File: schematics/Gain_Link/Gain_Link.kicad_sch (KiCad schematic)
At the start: 12 parts, among them IC1 AD8221TRMZ-EP, J1 PCIE-036-02-X-D-TH, J2 Conn_01x05_Socket

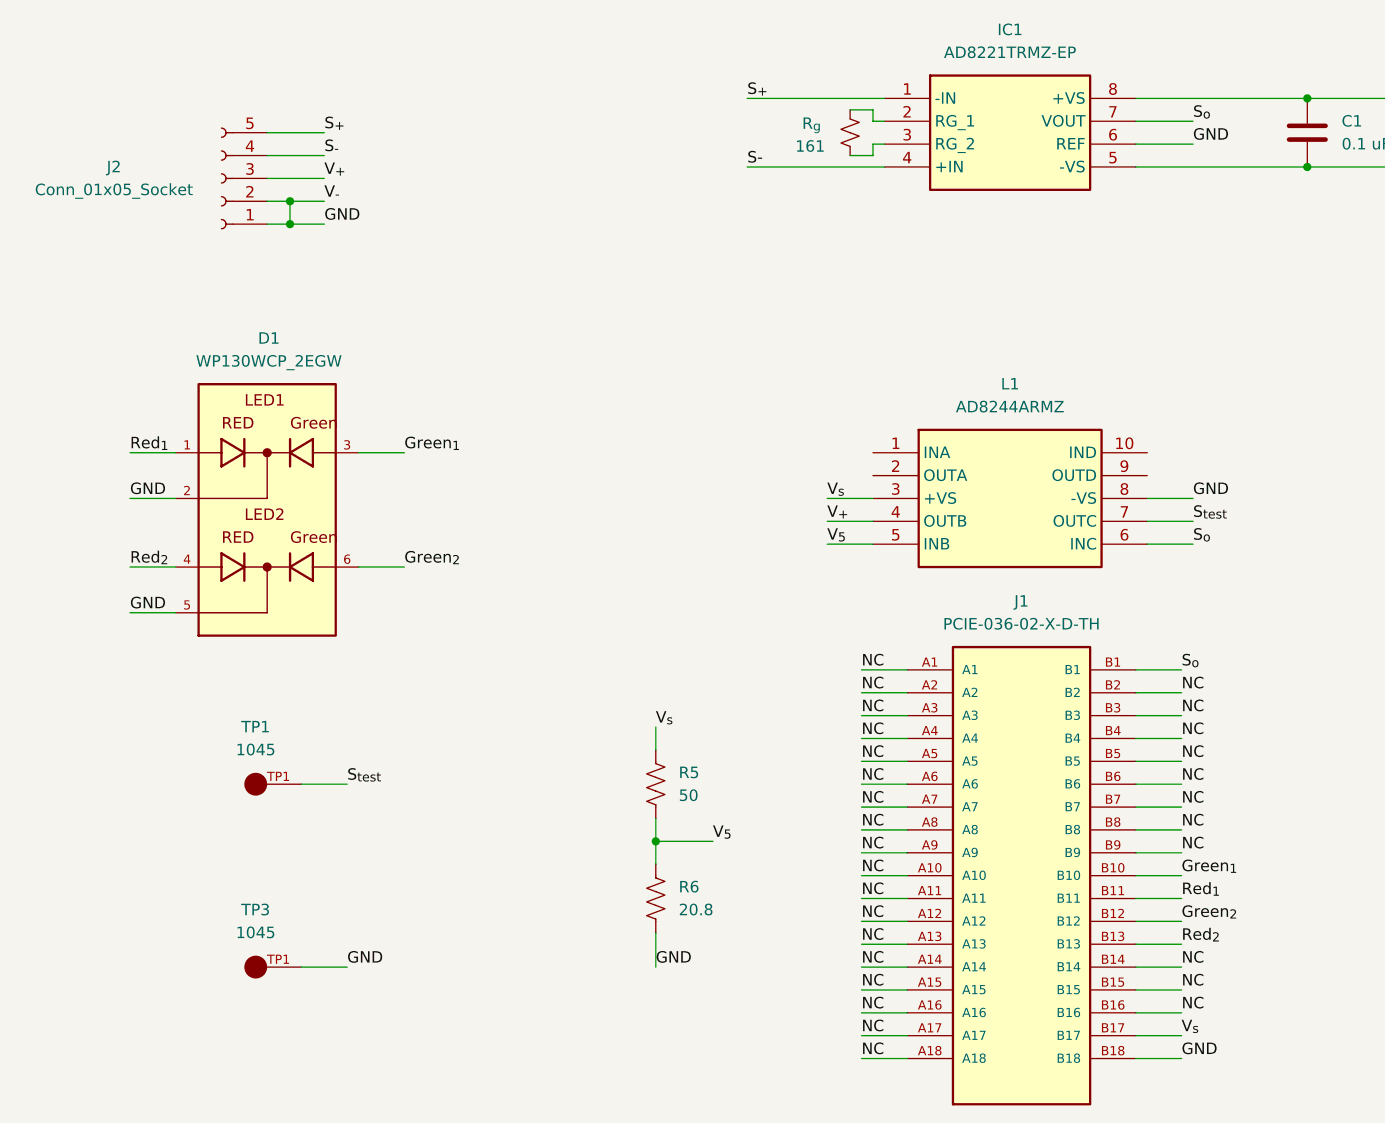
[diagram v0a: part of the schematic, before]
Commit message: Updated LP_breakout
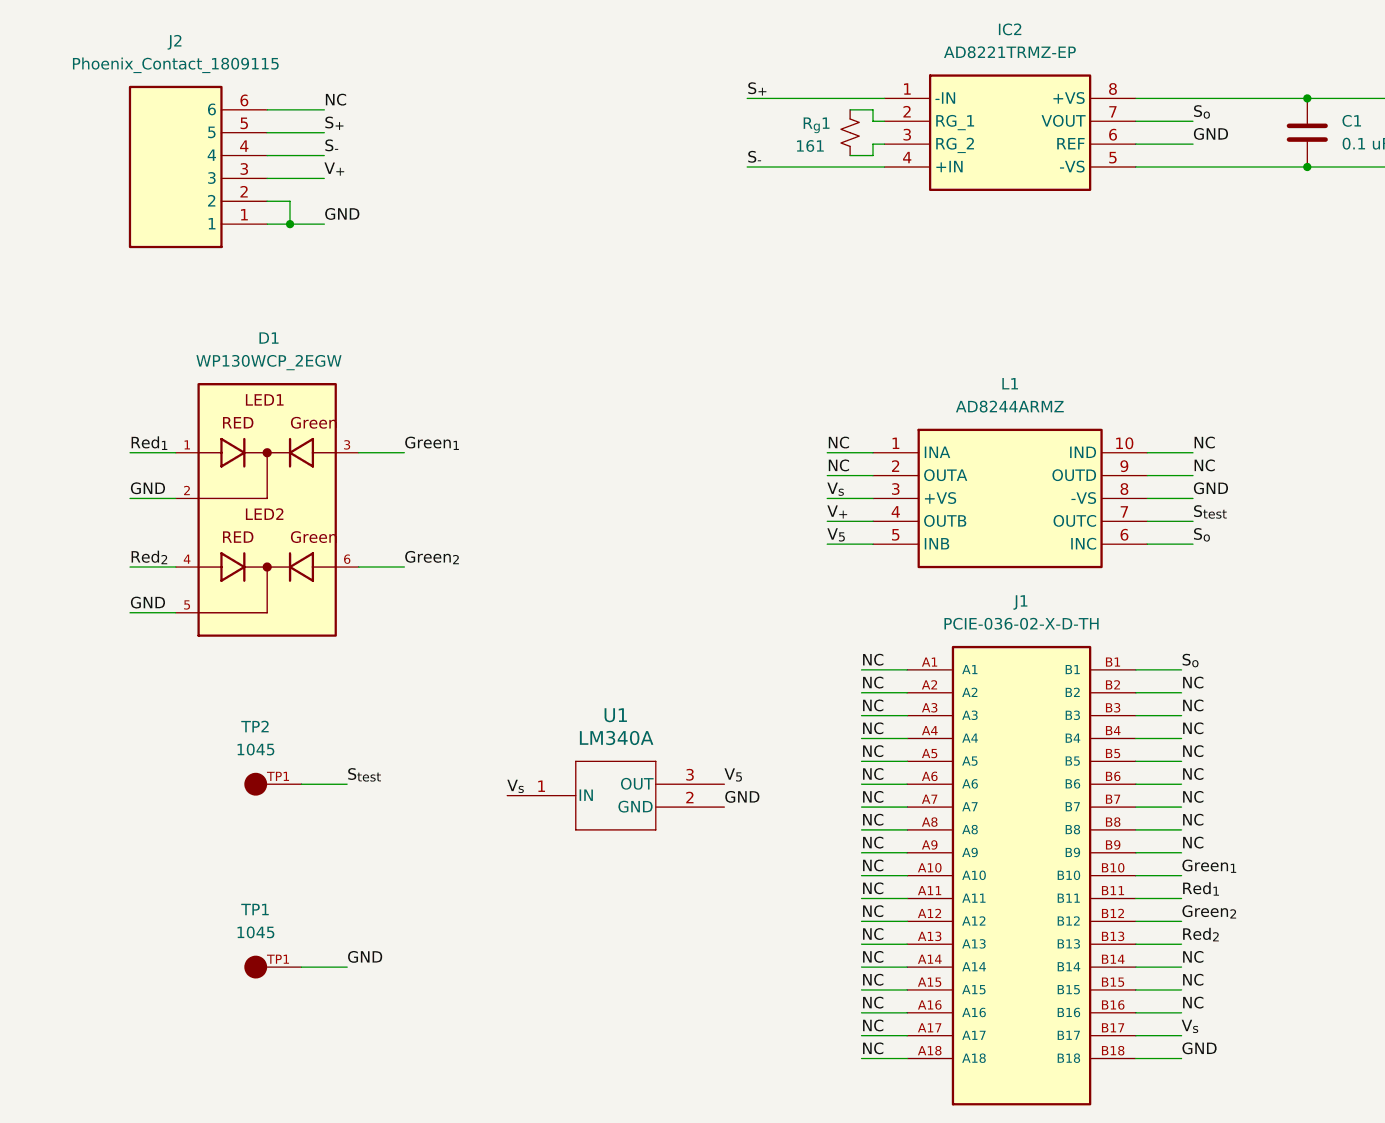
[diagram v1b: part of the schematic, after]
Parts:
- removed IC1: AD8221TRMZ-EP, Link_Footprints:AD8221TRMZ-EP, symbol Link_Components:AD8221TRMZ-EP
- removed J2: Conn_01x05_Socket, Link_Footprints:Phoenix_Contact_MSTBA,5-LR, symbol Connector:Conn_01x05_Socket
- removed R5: 50, Resistor_SMD:R_0805_2012Metric, symbol Device:R_US
- removed R6: 20.8, Resistor_SMD:R_0805_2012Metric, symbol Device:R_US
- removed TP3: 1045, Link_Footprints:Keystone_1045, symbol Link_Components:1045
- added IC2: AD8221TRMZ-EP, symbol Link_Components:AD8221TRMZ-EP
- added J2: Phoenix_Contact_1809115, symbol Link_Components:Phoenix_Contact_1809115
- added TP2: 1045, symbol Link_Components:1045
- added U1: LM340A, T03B_TEX, symbol Link_Components:LM340A
- D1: footprint Link_Footprints:LED_Lights -> (none)
- J1: footprint Link_Footprints:SAMTEC_PCIE_1x -> (none)
- L1: footprint Link_Footprints:AD8244ARMZ -> (none)
- TP1: footprint Link_Footprints:Keystone_1045 -> (none)
- renumbered R_{g} to R_{g}1
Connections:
- net GND: now also TP1.TP1, IC2.5 (-VS), IC2.6 (REF), J2.1, J2.2, U1.2 (GND)
- net NC: now also L1.1 (INA), L1.10 (IND), L1.2 (OUTA), L1.9 (OUTD), J2.6
- net S_{+}: now also IC2.1 (-IN), J2.5
- net S_{-}: now also IC2.4 (+IN), J2.4
- net S_{o}: now also IC2.7 (VOUT)
- net S_{test}: now also TP2.TP1; no longer TP1.TP1
- net V_{+}: now also J2.3
- net V_{5}: now also U1.3 (OUT)
- net V_{s}: now also IC2.8 (+VS), U1.1 (IN)
- net at R_{g}1.1: now also IC2.2 (RG_1)
- net at R_{g}1.2: now also IC2.3 (RG_2)

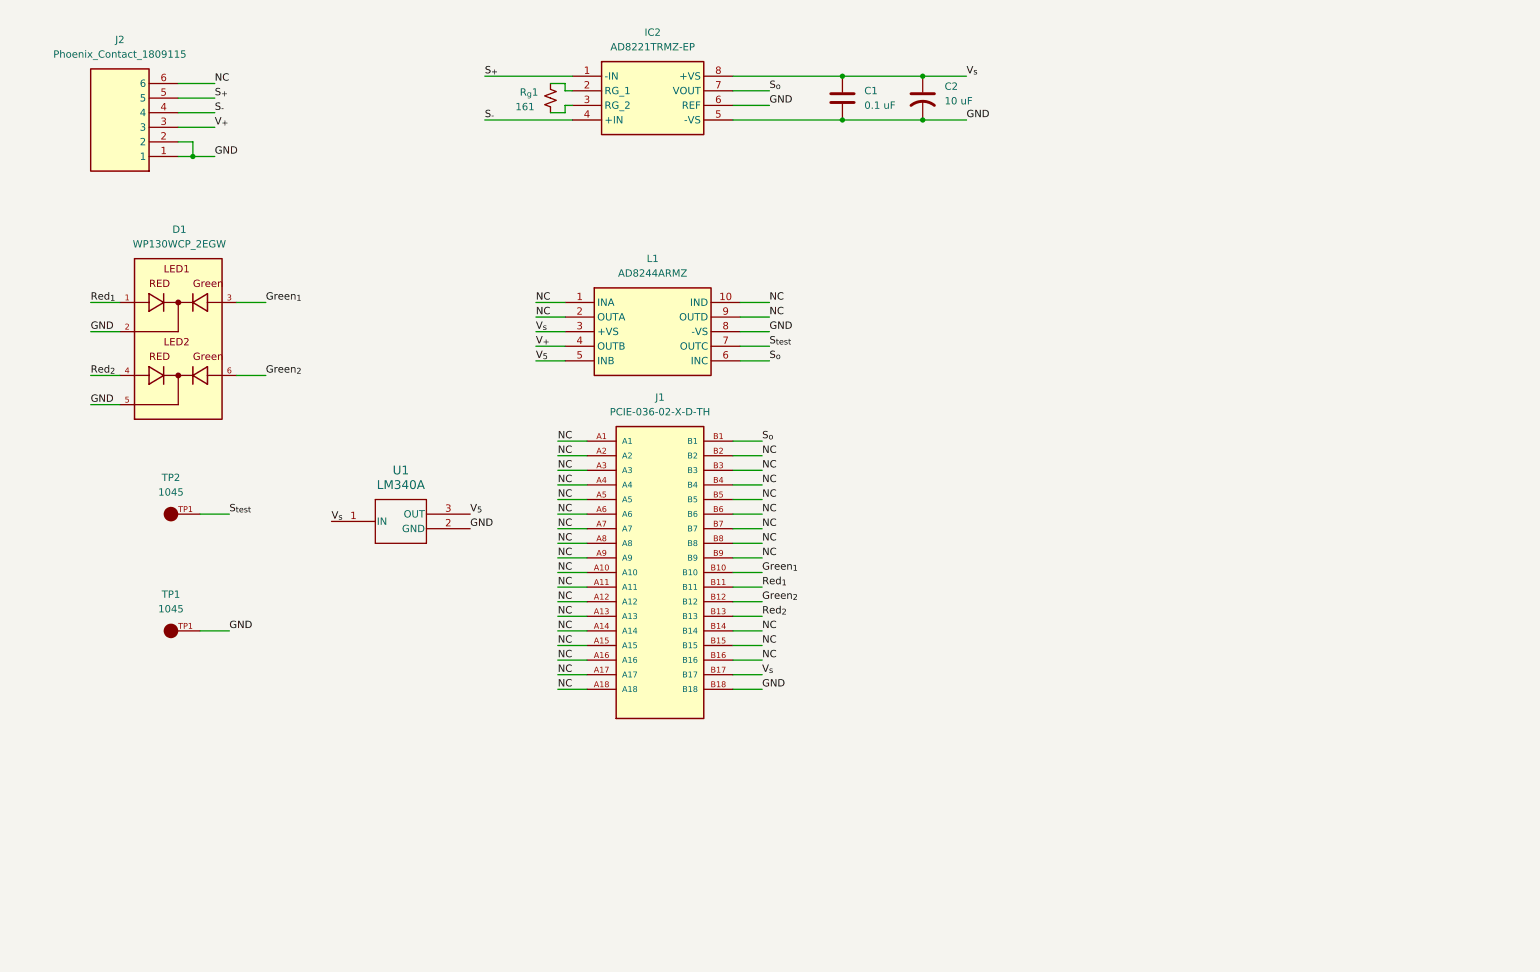
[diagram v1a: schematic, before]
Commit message: Match gain link schematic to shunt link`
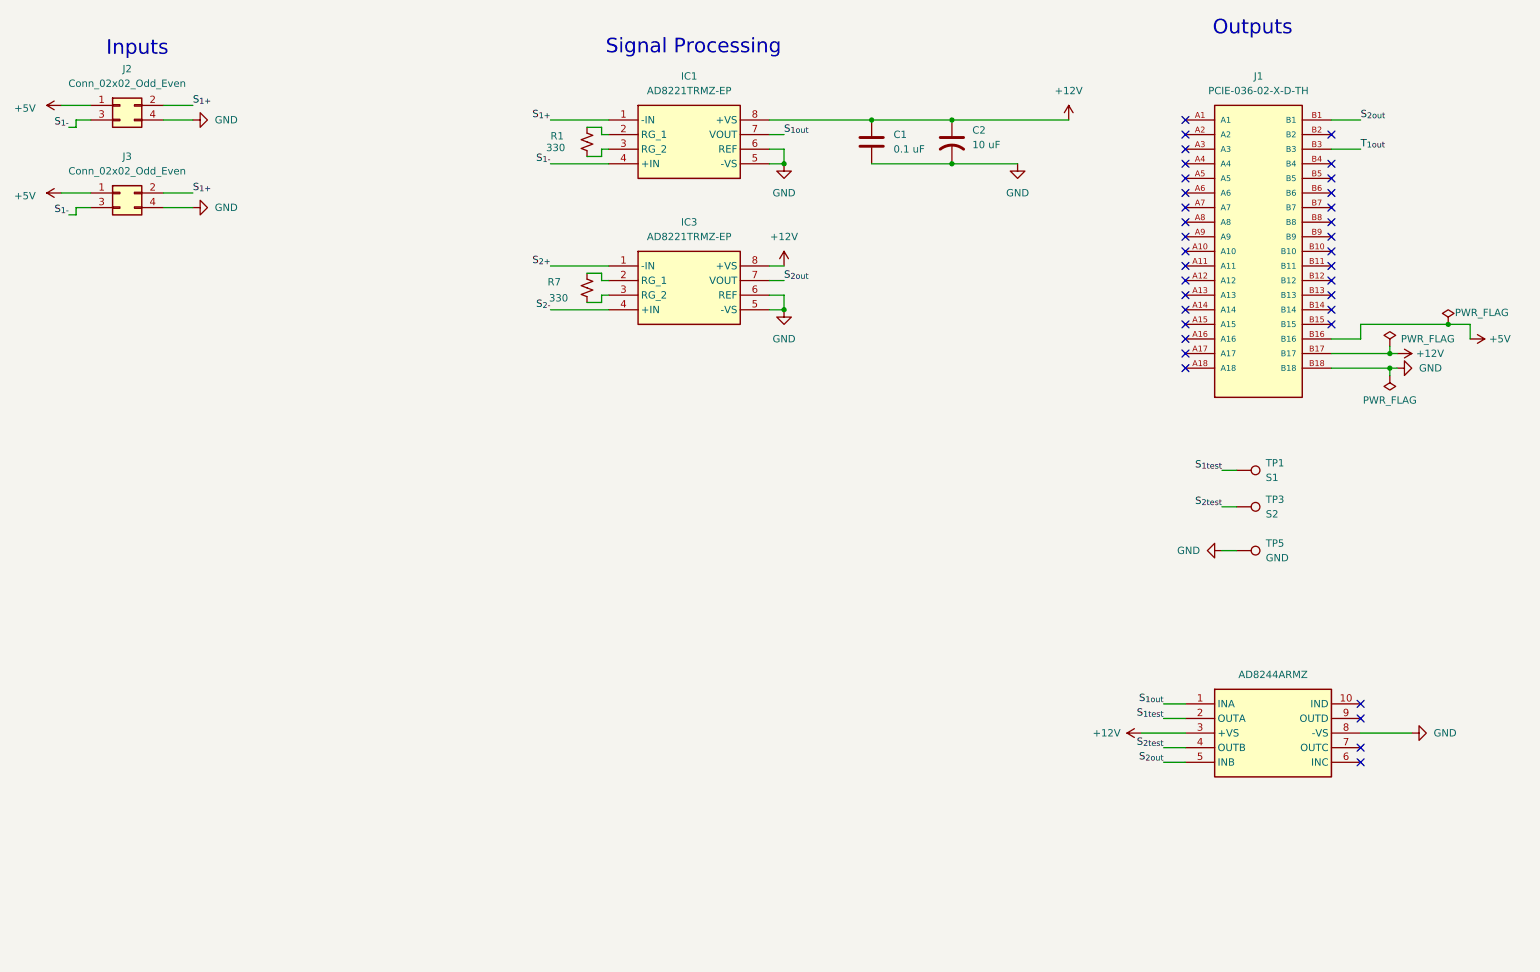
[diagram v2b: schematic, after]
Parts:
- removed D1: WP130WCP_2EGW, symbol Link_Components:WP130WCP_2EGW
- removed IC2: AD8221TRMZ-EP, symbol Link_Components:AD8221TRMZ-EP
- removed J2: Phoenix_Contact_1809115, symbol Link_Components:Phoenix_Contact_1809115
- removed R_{g}1: 161, Resistor_SMD:R_0805_2012Metric, symbol Device:R_Small_US
- removed TP1, TP2: 1045, symbol Link_Components:1045
- removed U1: LM340A, T03B_TEX, symbol Link_Components:LM340A
- added IC1, IC3: AD8221TRMZ-EP, Link_Footprints:AD8221TRMZ-EP, symbol Link_Components:AD8221TRMZ-EP
- added J2, J3: Conn_02x02_Odd_Even, symbol Connector_Generic:Conn_02x02_Odd_Even
- added R1, R7: 330, Resistor_SMD:R_2512_6332Metric, symbol Device:R_Small_US
- added TP1: S1, Link_Footprints:KEYSTONE_5017, symbol Connector:TestPoint
- added TP3: S2, Link_Footprints:KEYSTONE_5017, symbol Connector:TestPoint
- added TP5: GND, Link_Footprints:KEYSTONE_5017, symbol Connector:TestPoint
- C1, C2: footprint (none) -> Capacitor_SMD:C_1210_3225Metric
- J1: footprint (none) -> Connector_PCBEdge:BUS_PCIexpress_x1
- L1: footprint (none) -> Link_Footprints:AD8244ARMZ
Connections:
- net GND: now also IC1.5 (-VS), IC1.6 (REF), IC3.5 (-VS), IC3.6 (REF), J2.4 (Pin_4), J3.4 (Pin_4), TP5.1
- net Green_{1}: no longer names the net of J1.B10
- net Green_{2}: no longer names the net of J1.B12
- removed net NC: J1.A1, J1.A10, J1.A11, J1.A12, J1.A13, J1.A14, J1.A15, J1.A16, J1.A17, J1.A18, J1.A2, J1.A3, J1.A4, J1.A5, J1.A6, J1.A7, J1.A8, J1.A9, J1.B14, J1.B15, J1.B16, J1.B2, J1.B3, J1.B4, J1.B5, J1.B6, J1.B7, J1.B8, J1.B9, L1.1 (INA), L1.10 (IND), L1.2 (OUTA), L1.9 (OUTD)
- net Red_{1}: no longer names the net of J1.B11
- net Red_{2}: no longer names the net of J1.B13
- net S_{o}: no longer names the net of L1.6 (INC)
- net S_{o}: no longer J1.B1
- net S_{test}: no longer names the net of L1.7 (OUTC)
- net V_{+} renamed S_{2test}
- net S_{2test}: now also TP3.1
- net V_{5} renamed S_{2out}
- net S_{2out}: now also J1.B1, IC3.7 (VOUT)
- net V_{s} renamed +12V
- net +12V: now also IC1.8 (+VS), IC3.8 (+VS)
- new net: IC1.2 (RG_1), R1.1
- new net: IC1.3 (RG_2), R1.2
- new net: IC3.2 (RG_1), R7.1
- new net: IC3.3 (RG_2), R7.2
- new net +5V: J1.B16, J2.1 (Pin_1), J3.1 (Pin_1)
- new net S_{1+}: IC1.1 (-IN), J2.2 (Pin_2), J3.2 (Pin_2)
- new net S_{1-}: IC1.4 (+IN), J2.3 (Pin_3), J3.3 (Pin_3)
- new net S_{1out}: IC1.7 (VOUT), L1.1 (INA)
- new net S_{1test}: L1.2 (OUTA), TP1.1
- new net S_{2+}: IC3.1 (-IN)
- new net S_{2-}: IC3.4 (+IN)
- new net T_{1out}: J1.B3
- no-connect marks 0 -> 35
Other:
- note added: "Inputs"
- note added: "Outputs"
- note added: "Signal Processing"

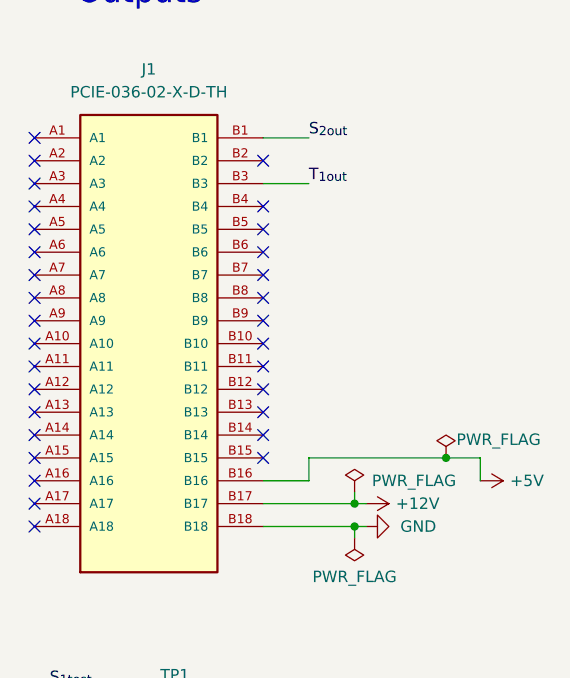
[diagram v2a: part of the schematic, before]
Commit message: Updated PCIe pinout
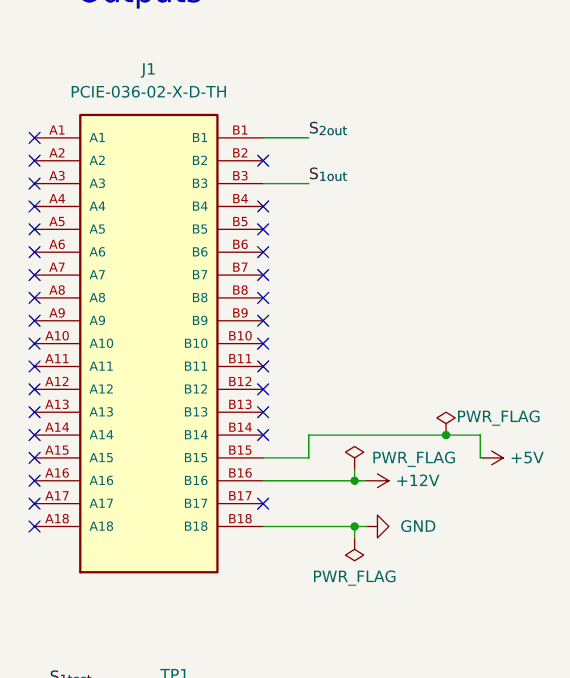
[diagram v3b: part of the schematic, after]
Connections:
- net T_{1out} is gone; now on net S_{1out}: J1.B3
- net +12V: now also J1.B16; no longer J1.B17
- net +5V: now also J1.B15; no longer J1.B16
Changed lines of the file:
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@@
 	)
 	(junction
-		(at 265.43 69.85)
+		(at 265.43 67.31)
 		(diameter 0)
 		(color 0 0 0 0)
 	)
 	(junction
-		(at 255.27 74.93)
+		(at 255.27 72.39)
 		(diameter 0)
 		(color 0 0 0 0)
@@
 	)
 	(no_connect
-		(at 219.71 64.77)
+		(at 245.11 74.93)
 	)
 	(no_connect
-		(at 219.71 67.31)
+		(at 219.71 64.77)
 	)
 	(no_connect
-		(at 245.11 69.85)
+		(at 219.71 67.31)
 	)
 	(no_connect
@@
 	(wire
 		(pts
-			(xy 255.27 73.66) (xy 255.27 74.93)
+			(xy 255.27 71.12) (xy 255.27 72.39)
 		)
 		(stroke
@@
 	(wire
 		(pts
-			(xy 269.24 69.85) (xy 265.43 69.85)
+			(xy 269.24 67.31) (xy 265.43 67.31)
 		)
 		(stroke
@@
 	(wire
 		(pts
-			(xy 250.19 69.85) (xy 250.19 72.39)
+			(xy 250.19 67.31) (xy 250.19 69.85)
 		)
 		(stroke
@@
 	(wire
 		(pts
-			(xy 269.24 69.85) (xy 269.24 72.39)
+			(xy 269.24 67.31) (xy 269.24 69.85)
 		)
 		(stroke
@@
 	(wire
 		(pts
-			(xy 256.54 74.93) (xy 255.27 74.93)
+			(xy 256.54 72.39) (xy 255.27 72.39)
 		)
 		(stroke
@@
 	(wire
 		(pts
-			(xy 250.19 69.85) (xy 265.43 69.85)
+			(xy 250.19 67.31) (xy 265.43 67.31)
 		)
 		(stroke
@@
 	(wire
 		(pts
-			(xy 250.19 72.39) (xy 245.11 72.39)
+			(xy 250.19 69.85) (xy 245.11 69.85)
 		)
 		(stroke
@@
 	(wire
 		(pts
-			(xy 245.11 74.93) (xy 255.27 74.93)
+			(xy 245.11 72.39) (xy 255.27 72.39)
 		)
 		(stroke
@@
 		)
 	)
-	(label "T_{1out}"
+	(label "S_{1out}"
 		(at 250.19 39.37 0)
 		(effects
@@
 	(symbol
 		(lib_id "power:+12V")
-		(at 256.54 74.93 270)
+		(at 256.54 72.39 270)
 		(unit 1)
 		(exclude_from_sim no)
@@
 		(dnp no)
 		(property "Reference" "#PWR04"
-			(at 252.73 74.93 0)
+			(at 252.73 72.39 0)
 			(effects
 				(font
@@
 		)
 		(property "Value" "+12V"
-			(at 259.842 74.93 90)
+			(at 259.842 72.39 90)
 			(effects
 				(font
@@
 		)
 		(property "Footprint" ""
-			(at 256.54 74.93 0)
+			(at 256.54 72.39 0)
 			(effects
 				(font
@@
 		)
 		(property "Datasheet" ""
-			(at 256.54 74.93 0)
+			(at 256.54 72.39 0)
 			(effects
 				(font
@@
 		)
 		(property "Description" "Power symbol creates a global label with name \"+12V\""
-			(at 256.54 74.93 0)
+			(at 256.54 72.39 0)
 			(effects
 				(font
@@
 	(symbol
 		(lib_id "power:PWR_FLAG")
-		(at 265.43 69.85 0)
+		(at 265.43 67.31 0)
 		(unit 1)
 		(exclude_from_sim no)
@@
 		(dnp no)
 		(property "Reference" "#FLG04"
-			(at 265.43 67.945 0)
+			(at 265.43 65.405 0)
 			(effects
 				(font
@@
 		)
 		(property "Value" "PWR_FLAG"
-			(at 271.272 67.818 0)
+			(at 271.272 65.278 0)
 			(effects
 				(font
@@
 		)
 		(property "Footprint" ""
-			(at 265.43 69.85 0)
+			(at 265.43 67.31 0)
 			(effects
 				(font
@@
 		)
 		(property "Datasheet" "~"
-			(at 265.43 69.85 0)
+			(at 265.43 67.31 0)
 			(effects
 				(font
@@
 		)
 		(property "Description" "Special symbol for telling ERC where power comes from"
-			(at 265.43 69.85 0)
+			(at 265.43 67.31 0)
 			(effects
 				(font
@@
 	(symbol
 		(lib_id "power:+12V")
-		(at 269.24 72.39 270)
+		(at 269.24 69.85 270)
 		(unit 1)
 		(exclude_from_sim no)
@@
 		(dnp no)
 		(property "Reference" "#PWR09"
-			(at 265.43 72.39 0)
+			(at 265.43 69.85 0)
 			(effects
 				(font
@@
 		)
 		(property "Value" "+5V"
-			(at 272.542 72.39 90)
+			(at 272.542 69.85 90)
 			(effects
 				(font
@@
 		)
 		(property "Footprint" ""
-			(at 269.24 72.39 0)
+			(at 269.24 69.85 0)
 			(effects
 				(font
@@
 		)
 		(property "Datasheet" ""
-			(at 269.24 72.39 0)
+			(at 269.24 69.85 0)
 			(effects
 				(font
@@
 		)
 		(property "Description" "Power symbol creates a global label with name \"+12V\""
-			(at 269.24 72.39 0)
+			(at 269.24 69.85 0)
 			(effects
 				(font
@@
 	(symbol
 		(lib_id "power:PWR_FLAG")
-		(at 255.27 73.66 0)
+		(at 255.27 71.12 0)
 		(unit 1)
 		(exclude_from_sim no)
@@
 		(dnp no)
 		(property "Reference" "#FLG02"
-			(at 255.27 71.755 0)
+			(at 255.27 69.215 0)
 			(effects
 				(font
@@
 		)
 		(property "Value" "PWR_FLAG"
-			(at 261.874 72.39 0)
+			(at 261.874 69.85 0)
 			(effects
 				(font
@@
 		)
 		(property "Footprint" ""
-			(at 255.27 73.66 0)
+			(at 255.27 71.12 0)
 			(effects
 				(font
@@
 		)
 		(property "Datasheet" "~"
-			(at 255.27 73.66 0)
+			(at 255.27 71.12 0)
 			(effects
 				(font
@@
 		)
 		(property "Description" "Special symbol for telling ERC where power comes from"
-			(at 255.27 73.66 0)
+			(at 255.27 71.12 0)
 			(effects
 				(font
